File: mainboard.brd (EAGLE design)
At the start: 90.2 x 95.9 mm, 69 parts, among them J1 POWER_JACKPTH_LOCK, T1 SINGLE_NCHAN_FET, T2 MOSFET_PCHAN_20A, T3 SINGLE_NCHAN_FET, T4 MOSFET_PCHAN_20A, T5 SINGLE_NCHAN_FET, T6 MOSFET_PCHAN_20A, T7 MOSFET_PCHAN_20A, T8 SINGLE_NCHAN_FET, U1 MURATA_REG_OKL-T3-W12, U2 TEENSY_3.0+4, U3 RFM23BP, U4 HMC5883LSMD, U5 ITG-3200, U7 CURRENT_MAX4372, U8 CURRENT_MAX4372

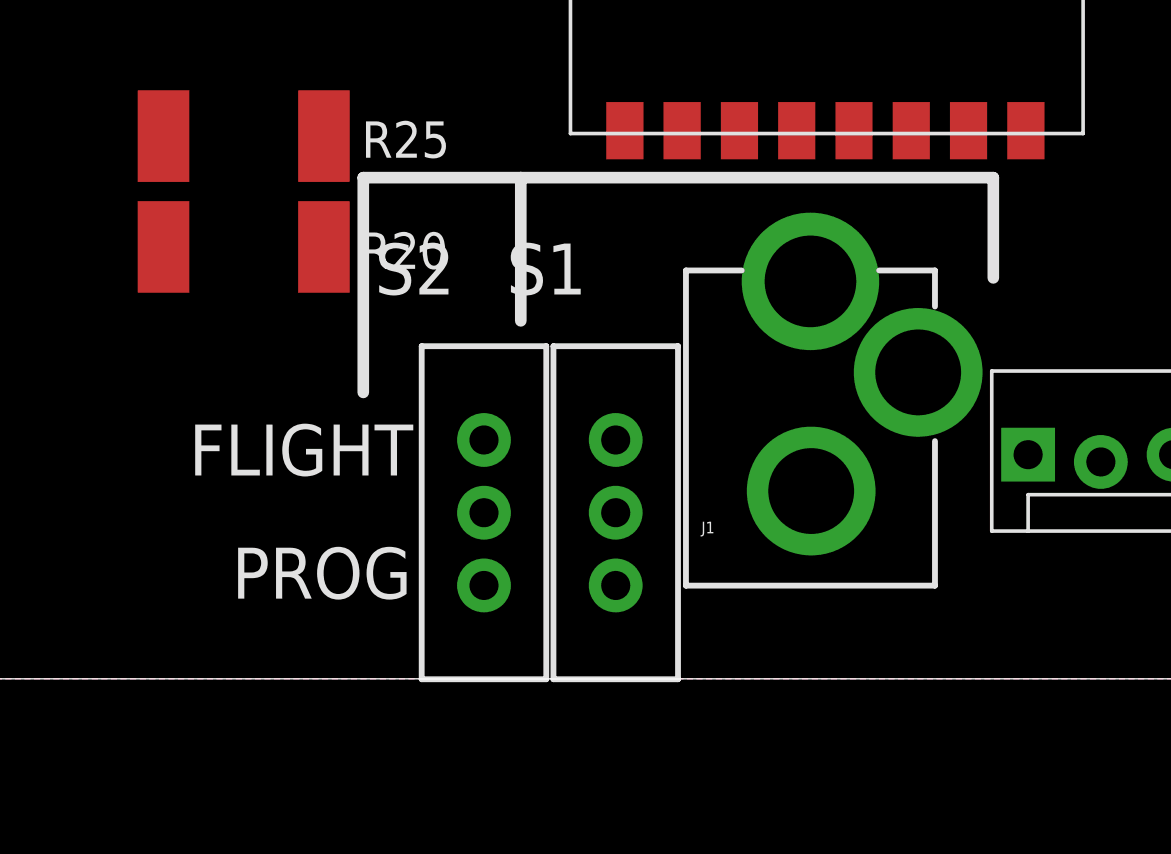
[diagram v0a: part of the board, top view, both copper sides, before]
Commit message: DPDT Switch for programming mode
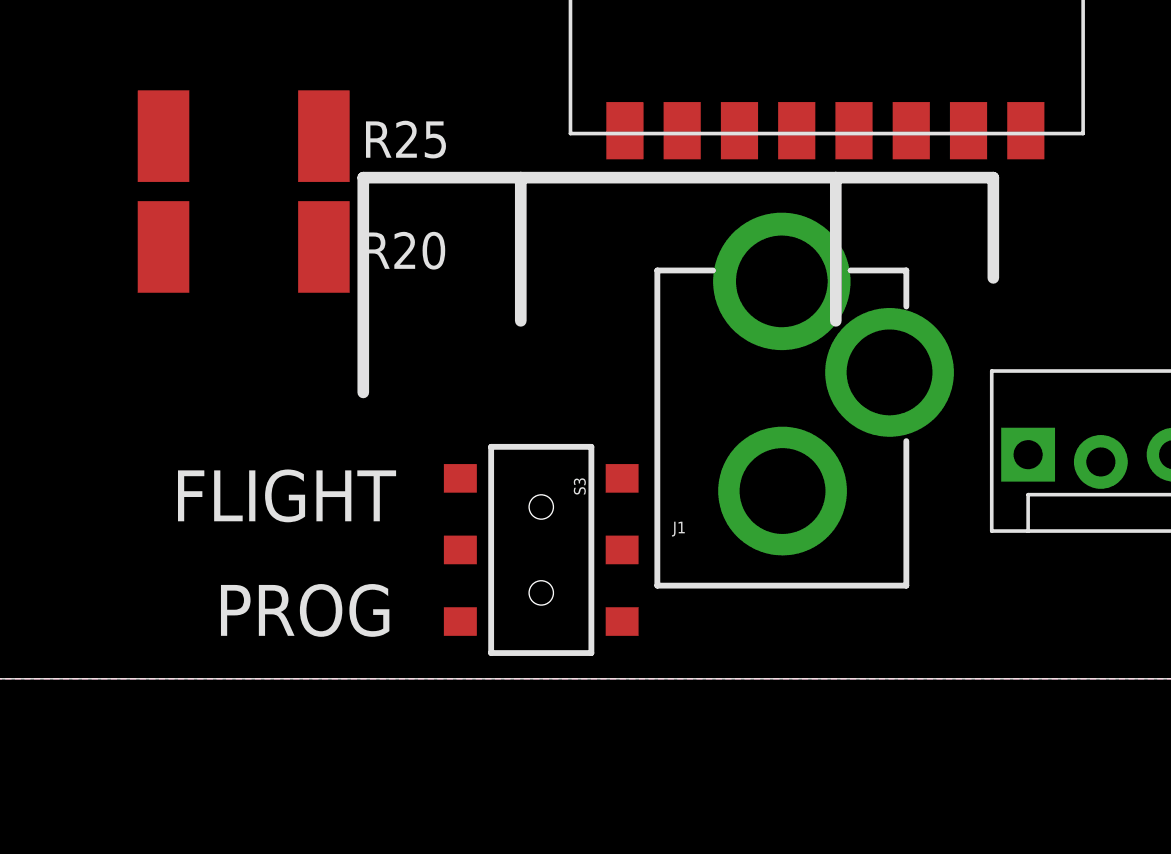
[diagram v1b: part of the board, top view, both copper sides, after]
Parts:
- removed S1, S2: (no value), SparkFun-Electromechanical:SWITCH-SPDT
- added S3: DPDT, SparkFun-Electromechanical:AYZ0202
- R14: value 10k -> 4.7k
- moved J1 1.00 mm to (48.7, 0.00)
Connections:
- net N$11: now also S3.3; no longer S1.2
- net N$13: now also S3.6; no longer S2.2
- net PGM_RST: now also S3.2; no longer S1.3
- net PGM_VCC: now also S3.5; no longer S2.3
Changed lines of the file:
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@@
 <wire x1="34.085" y1="10" x2="34.085" y2="17.5" width="0.4064" layer="21"/>
 <wire x1="34.085" y1="17.5" x2="39.585" y2="17.5" width="0.4064" layer="21"/>
-<wire x1="39.585" y1="17.5" x2="56.085" y2="17.5" width="0.4064" layer="21"/>
+<wire x1="39.585" y1="17.5" x2="50.585" y2="17.5" width="0.4064" layer="21"/>
+<wire x1="50.585" y1="17.5" x2="56.085" y2="17.5" width="0.4064" layer="21"/>
 <wire x1="56.085" y1="17.5" x2="56.085" y2="14" width="0.4064" layer="21"/>
 <wire x1="34.085" y1="95.885" x2="34.085" y2="78.385" width="0.4064" layer="21"/>
 <wire x1="56.085" y1="78.385" x2="56.085" y2="95.885" width="0.4064" layer="21"/>
-<text x="29.5" y="2.8" size="1.778" layer="21">PROG</text>
-<text x="28" y="7.1" size="1.778" layer="21">FLIGHT</text>
+<text x="28.9" y="1.5" size="1.778" layer="21">PROG</text>
+<text x="27.4" y="5.5" size="1.778" layer="21">FLIGHT</text>
+<wire x1="50.585" y1="12.5" x2="50.585" y2="17.5" width="0.4064" layer="21"/>
 </plain>
 <attributes>
@@
 <element name="R12" library="SparkFun-Resistors" package="0805" value="10K" x="-57" y="-62.4"/>
 <element name="R13" library="SparkFun-Resistors" package="0805" value="4.7K" x="-54" y="-62.4"/>
-<element name="J1" library="SparkFun-Connectors" package="POWER_JACK_PTH_LOCK" value="POWER_JACKPTH_LOCK" x="49.7" y="0">
-<attribute name="PROD_ID" value="PRT-00119" x="49.7" y="0" size="1.778" layer="27" display="off"/>
+<element name="J1" library="SparkFun-Connectors" package="POWER_JACK_PTH_LOCK" value="POWER_JACKPTH_LOCK" x="48.7" y="0">
+<attribute name="PROD_ID" value="PRT-00119" x="48.7" y="0" size="1.778" layer="27" display="off"/>
 </element>
 <element name="U$3" library="SparkFun-Boards" package="ARDUINO_PRO_MINI" value="ARDUINO_PRO_MINI" x="74" y="25" rot="R180"/>
-<element name="R14" library="SparkFun-Resistors" package="0805" value="10k" x="-95.9" y="-62.4"/>
-<element name="S1" library="SparkFun-Electromechanical" package="SWITCH-SPDT" value="" x="42.9" y="5.8"/>
-<element name="S2" library="SparkFun-Electromechanical" package="SWITCH-SPDT" value="" x="38.3" y="5.8"/>
+<element name="R14" library="SparkFun-Resistors" package="0805" value="4.7k" x="-95.9" y="-62.4"/>
+<element name="S3" library="SparkFun-Electromechanical" package="AYZ0202" value="DPDT" x="40.3" y="4.5" rot="R270">
+<attribute name="PROD_ID" value="SWCH-08179" x="40.3" y="4.5" size="1.778" layer="27" rot="R270" display="off"/>
+</element>
 </elements>
 <signals>
@@
 <contactref element="ST1" pad="1"/>
 <contactref element="J1" pad="PWR"/>
-<wire x1="19.23" y1="13.9322" x2="49.7" y2="13.8778" width="0" layer="19" extent="1-1"/>
+<wire x1="19.23" y1="13.9322" x2="48.7" y2="13.8778" width="0" layer="19" extent="1-1"/>
 <wire x1="12.09" y1="17.7878" x2="19.23" y2="13.9322" width="0" layer="19" extent="1-1"/>
 <wire x1="12.09" y1="24.7878" x2="12.09" y2="17.7878" width="0" layer="19" extent="1-1"/>
@@
 <contactref element="J1" pad="GNDBREAK"/>
 <contactref element="J1" pad="GND"/>
-<wire x1="49.7254" y1="6.557" x2="53.4616" y2="10.7" width="0" layer="19" extent="1-1"/>
-<wire x1="12.6222" y1="8" x2="49.7254" y2="6.557" width="0" layer="19" extent="1-1"/>
+<wire x1="48.7254" y1="6.557" x2="52.4616" y2="10.7" width="0" layer="19" extent="1-1"/>
+<wire x1="12.6222" y1="8" x2="48.7254" y2="6.557" width="0" layer="19" extent="1-1"/>
 <wire x1="12.09" y1="13.9322" x2="12.6222" y2="8" width="0" layer="19" extent="1-1"/>
 <wire x1="12.09" y1="20.9322" x2="12.09" y2="13.9322" width="0" layer="19" extent="1-1"/>
@@
 <signal name="PGM_VCC">
 <contactref element="U$3" pad="21"/>
-<contactref element="S2" pad="3"/>
-<wire x1="38.3" y1="3.26" x2="66.38" y2="19.92" width="0" layer="19" extent="1-1"/>
+<contactref element="S3" pad="5"/>
+<wire x1="66.38" y1="19.92" x2="37.475" y2="4.5" width="0" layer="19" extent="1-1"/>
 </signal>
 <signal name="N$11">
 <contactref element="U2" pad="23/A9"/>
-<contactref element="S1" pad="2"/>
-<wire x1="42.9" y1="5.8" x2="52.705" y2="85.89" width="0" layer="19" extent="1-1"/>
+<contactref element="S3" pad="3"/>
+<wire x1="52.705" y1="85.89" x2="43.125" y2="2" width="0" layer="19" extent="1-1"/>
 </signal>
 <signal name="PGM_RST">
 <contactref element="U$3" pad="22"/>
-<contactref element="S1" pad="3"/>
-<wire x1="42.9" y1="3.26" x2="66.38" y2="17.38" width="0" layer="19" extent="1-1"/>
+<contactref element="S3" pad="2"/>
+<wire x1="66.38" y1="17.38" x2="43.125" y2="4.5" width="0" layer="19" extent="1-1"/>
 </signal>
 <signal name="N$13">
-<contactref element="S2" pad="2"/>
 <contactref element="U2" pad="VUSB"/>
-<wire x1="38.3" y1="5.8" x2="50.165" y2="90.97" width="0" layer="19" extent="1-1"/>
+<contactref element="S3" pad="6"/>
+<wire x1="50.165" y1="90.97" x2="37.475" y2="2" width="0" layer="19" extent="1-1"/>
 </signal>
 </signals>

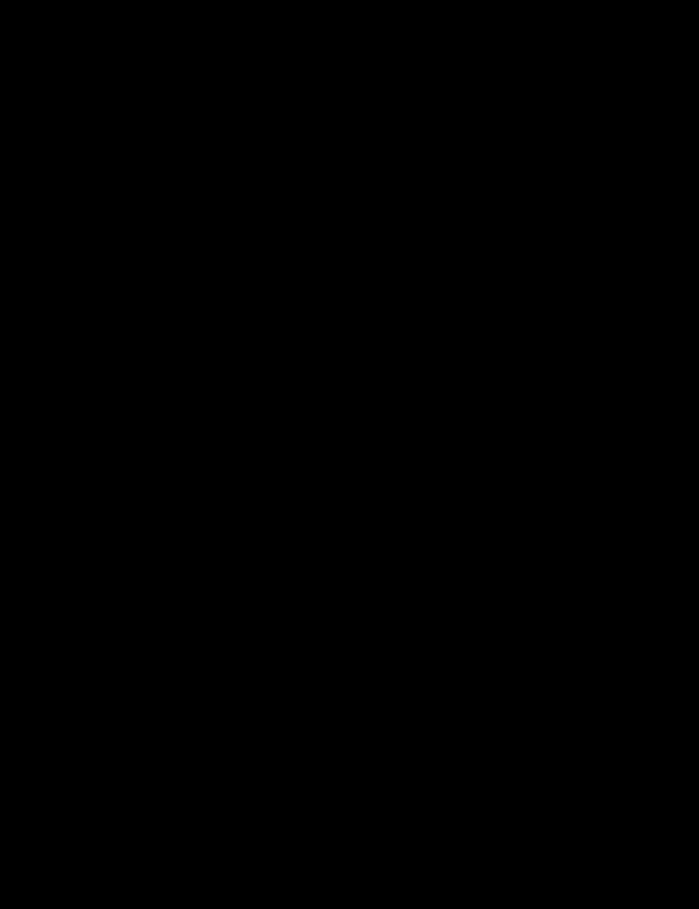
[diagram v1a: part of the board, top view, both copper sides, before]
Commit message: added piksi gps connector and enable circuitry. Added molex library
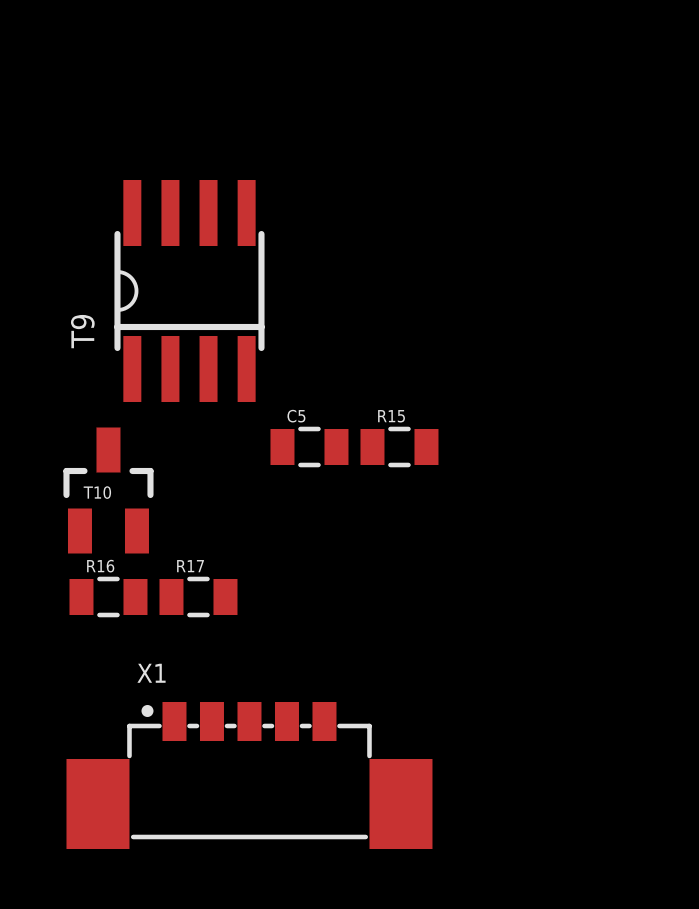
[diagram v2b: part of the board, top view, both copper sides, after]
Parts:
- added C5: .1uF, SparkFun-Capacitors:0805
- added R15: 3K3, SparkFun-Resistors:0805
- added R16: 10K, SparkFun-Resistors:0805
- added R17: 4.7K, SparkFun-Resistors:0805
- added T10: SINGLE_NCHAN_FET, phonesat:SOT23-3
- added T9: MOSFET_PCHAN_20A, phonesat:SO8
- added X1: (no value), pel_molex:PB-53398-05
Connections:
- new net ENAB_GPS: R16.1, R17.2, U2.17/A3
- new net GPS_PWR: T9.5, T9.6, T9.7, T9.8, X1.5
- new net N$10: C5.1, R16.2, T10.1
- new net N$12: R15.1, T10.3, T9.4
- net 5V: now also R15.2, T9.1, T9.2, T9.3
- net GND: now also C5.2, R17.1, T10.2, X1.1
- net UART3_RX: now also X1.3
- net UART3_TX: now also X1.2

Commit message: Schematic clean-up
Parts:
- added FRAME1, FRAME2, FRAME3: FRAME-LETTER, SparkFun-Aesthetics:CREATIVE_COMMONS
- X1: device pel_molex:PB-53398-05 -> pel_molex:PB-53261-05
- moved T9 32.7 mm to (-93.2, -106.9)
- moved C5 32.7 mm to (-89.2, -112.1)
- moved R15 32.7 mm to (-86.2, -112.1)
- moved R16 32.7 mm to (-95.9, -117.1)
- moved R17 32.7 mm to (-92.9, -117.1)
- moved T10 32.7 mm to (-95.9, -113.6)
- moved X1 22.0 mm to (-91.2, -67.8)
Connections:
- net N$11: now also S3.1; no longer S3.3
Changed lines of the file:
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@@
 <attribute name="PROD_ID" value="SWCH-08179" x="40.3" y="4.5" size="1.778" layer="27" rot="R270" display="off"/>
 </element>
-<element name="T9" library="phonesat" package="SO8" value="MOSFET_PCHAN_20A" x="-93.2" y="-74.2"/>
-<element name="T10" library="phonesat" package="SOT23-3" value="SINGLE_NCHAN_FET" x="-95.9" y="-80.9"/>
-<element name="R15" library="SparkFun-Resistors" package="0805" value="3K3" x="-86.2" y="-79.4"/>
-<element name="C5" library="SparkFun-Capacitors" package="0805" value=".1uF" x="-89.2" y="-79.4"/>
-<element name="R16" library="SparkFun-Resistors" package="0805" value="10K" x="-95.9" y="-84.4"/>
-<element name="R17" library="SparkFun-Resistors" package="0805" value="4.7K" x="-92.9" y="-84.4"/>
-<element name="X1" library="pel_molex" package="PB-53398-05" value="" x="-91.2" y="-89.8"/>
+<element name="X1" library="pel_molex" package="PB-53261-05" value="" x="-91.2" y="-67.8"/>
+<element name="FRAME1" library="SparkFun-Aesthetics" package="CREATIVE_COMMONS" value="FRAME-LETTER" x="-76.5" y="-79"/>
+<element name="FRAME2" library="SparkFun-Aesthetics" package="CREATIVE_COMMONS" value="FRAME-LETTER" x="-76.5" y="-87.5"/>
+<element name="FRAME3" library="SparkFun-Aesthetics" package="CREATIVE_COMMONS" value="FRAME-LETTER" x="-76.5" y="-96"/>
+<element name="T9" library="phonesat" package="SO8" value="MOSFET_PCHAN_20A" x="-93.2" y="-106.9"/>
+<element name="T10" library="phonesat" package="SOT23-3" value="SINGLE_NCHAN_FET" x="-95.9" y="-113.6"/>
+<element name="R15" library="SparkFun-Resistors" package="0805" value="3K3" x="-86.2" y="-112.1"/>
+<element name="C5" library="SparkFun-Capacitors" package="0805" value=".1uF" x="-89.2" y="-112.1"/>
+<element name="R16" library="SparkFun-Resistors" package="0805" value="10K" x="-95.9" y="-117.1"/>
+<element name="R17" library="SparkFun-Resistors" package="0805" value="4.7K" x="-92.9" y="-117.1"/>
 </elements>
 <signals>
@@
 <contactref element="U$3" pad="4"/>
 <contactref element="R14" pad="1"/>
+<contactref element="X1" pad="1"/>
 <contactref element="T10" pad="2"/>
 <contactref element="C5" pad="2"/>
 <contactref element="R17" pad="1"/>
-<contactref element="X1" pad="1"/>
-<wire x1="-93.8" y1="-84.4" x2="-93.7" y2="-88.55" width="0" layer="19" extent="1-1"/>
-<wire x1="-94.95" y1="-82.2" x2="-93.8" y2="-84.4" width="0" layer="19" extent="1-1"/>
-<wire x1="-88.3" y1="-79.4" x2="-94.95" y2="-82.2" width="0" layer="19" extent="1-1"/>
-<wire x1="-96.8" y1="-62.4" x2="-88.3" y2="-79.4" width="0" layer="19" extent="1-1"/>
-<wire x1="-54.9" y1="-62.4" x2="-88.3" y2="-79.4" width="0" layer="19" extent="1-1"/>
-<wire x1="-56.05" y1="-60.2" x2="-54.9" y2="-62.4" width="0" layer="19" extent="1-1"/>
+<wire x1="-93.8" y1="-117.1" x2="-94.95" y2="-114.9" width="0" layer="19" extent="1-1"/>
+<wire x1="-88.3" y1="-112.1" x2="-94.95" y2="-114.9" width="0" layer="19" extent="1-1"/>
+<wire x1="-93.7" y1="-66.7" x2="-88.3" y2="-112.1" width="0" layer="19" extent="1-1"/>
+<wire x1="-96.8" y1="-62.4" x2="-93.7" y2="-66.7" width="0" layer="19" extent="1-1"/>
+<wire x1="-56.05" y1="-60.2" x2="-93.7" y2="-66.7" width="0" layer="19" extent="1-1"/>
+<wire x1="-54.9" y1="-62.4" x2="-56.05" y2="-60.2" width="0" layer="19" extent="1-1"/>
 <wire x1="-49.4" y1="-57.4" x2="-56.05" y2="-60.2" width="0" layer="19" extent="1-1"/>
 <wire x1="-52.3" y1="1.8" x2="-49.4" y2="-57.4" width="0" layer="19" extent="1-1"/>
@@
 <wire x1="59.43" y1="72" x2="61.37" y2="73.81" width="0" layer="19" extent="1-1"/>
 <wire x1="63.43" y1="66.79" x2="63" y2="70.47" width="0" layer="19" extent="1-1"/>
+<wire x1="42.545" y1="60.49" x2="59.43" y2="72" width="0" layer="19" extent="1-1"/>
 <wire x1="27.08" y1="30.4901" x2="42.545" y2="60.49" width="0" layer="19" extent="1-1"/>
 <wire x1="25.47" y1="30.49" x2="27.08" y2="30.4901" width="0" layer="19" extent="1-1"/>
@@
 <contactref element="T9" pad="2"/>
 <contactref element="R15" pad="2"/>
-<wire x1="-93.835" y1="-76.8" x2="-95.105" y2="-76.8" width="0" layer="19" extent="1-1"/>
-<wire x1="-92.565" y1="-76.8" x2="-93.835" y2="-76.8" width="0" layer="19" extent="1-1"/>
-<wire x1="-85.3" y1="-79.4" x2="-92.565" y2="-76.8" width="0" layer="19" extent="1-1"/>
-<wire x1="51.22" y1="19.14" x2="-85.3" y2="-79.4" width="0" layer="19" extent="1-1"/>
+<wire x1="-93.835" y1="-109.5" x2="-95.105" y2="-109.5" width="0" layer="19" extent="1-1"/>
+<wire x1="-92.565" y1="-109.5" x2="-93.835" y2="-109.5" width="0" layer="19" extent="1-1"/>
+<wire x1="-85.3" y1="-112.1" x2="-92.565" y2="-109.5" width="0" layer="19" extent="1-1"/>
+<wire x1="51.22" y1="19.14" x2="-85.3" y2="-112.1" width="0" layer="19" extent="1-1"/>
 <wire x1="21.7" y1="70.5" x2="51.22" y2="19.14" width="0" layer="19" extent="1-1"/>
 <wire x1="21.629" y1="74.039" x2="21.7" y2="70.5" width="0" layer="19" extent="1-1"/>
@@
 <contactref element="U2" pad="7"/>
 <contactref element="X1" pad="3"/>
-<wire x1="37.465" y1="73.19" x2="-91.2" y2="-88.55" width="0" layer="19" extent="1-1"/>
+<wire x1="37.465" y1="73.19" x2="-91.2" y2="-66.7" width="0" layer="19" extent="1-1"/>
 </signal>
 <signal name="UART3_TX">
 <contactref element="U2" pad="8"/>
 <contactref element="X1" pad="2"/>
-<wire x1="37.465" y1="70.65" x2="-92.45" y2="-88.55" width="0" layer="19" extent="1-1"/>
+<wire x1="37.465" y1="70.65" x2="-92.45" y2="-66.7" width="0" layer="19" extent="1-1"/>
 </signal>
 <signal name="RF_SDN">
@@
 <signal name="N$11">
 <contactref element="U2" pad="23/A9"/>
-<contactref element="S3" pad="3"/>
-<wire x1="52.705" y1="85.89" x2="43.125" y2="2" width="0" layer="19" extent="1-1"/>
+<contactref element="S3" pad="1"/>
+<wire x1="43.125" y1="7" x2="52.705" y2="85.89" width="0" layer="19" extent="1-1"/>
 </signal>
 <signal name="PGM_RST">
@@
 <contactref element="U2" pad="VUSB"/>
 <contactref element="S3" pad="6"/>
-<wire x1="50.165" y1="90.97" x2="37.475" y2="2" width="0" layer="19" extent="1-1"/>
+<wire x1="37.475" y1="2" x2="50.165" y2="90.97" width="0" layer="19" extent="1-1"/>
 </signal>
 <signal name="N$10">
@@
 <contactref element="C5" pad="1"/>
 <contactref element="T10" pad="1"/>
-<wire x1="-96.85" y1="-82.2" x2="-95" y2="-84.4" width="0" layer="19" extent="1-1"/>
-<wire x1="-90.1" y1="-79.4" x2="-95" y2="-84.4" width="0" layer="19" extent="1-1"/>
+<wire x1="-96.85" y1="-114.9" x2="-95" y2="-117.1" width="0" layer="19" extent="1-1"/>
+<wire x1="-90.1" y1="-112.1" x2="-95" y2="-117.1" width="0" layer="19" extent="1-1"/>
 </signal>
 <signal name="N$12">
@@
 <contactref element="T9" pad="4"/>
 <contactref element="R15" pad="1"/>
-<wire x1="-91.295" y1="-76.8" x2="-95.9" y2="-79.5" width="0" layer="19" extent="1-1"/>
-<wire x1="-87.1" y1="-79.4" x2="-91.295" y2="-76.8" width="0" layer="19" extent="1-1"/>
+<wire x1="-91.295" y1="-109.5" x2="-95.9" y2="-112.2" width="0" layer="19" extent="1-1"/>
+<wire x1="-87.1" y1="-112.1" x2="-91.295" y2="-109.5" width="0" layer="19" extent="1-1"/>
 </signal>
 <signal name="ENAB_GPS">
@@
 <contactref element="R17" pad="2"/>
 <contactref element="U2" pad="17/A3"/>
-<wire x1="-92" y1="-84.4" x2="-96.8" y2="-84.4" width="0" layer="19" extent="1-1"/>
-<wire x1="52.705" y1="70.65" x2="-92" y2="-84.4" width="0" layer="19" extent="1-1"/>
+<wire x1="-92" y1="-117.1" x2="-96.8" y2="-117.1" width="0" layer="19" extent="1-1"/>
+<wire x1="52.705" y1="70.65" x2="-92" y2="-117.1" width="0" layer="19" extent="1-1"/>
 </signal>
 <signal name="GPS_PWR">
@@
 <contactref element="T9" pad="5"/>
 <contactref element="X1" pad="5"/>
-<wire x1="-91.295" y1="-71.6" x2="-88.7" y2="-88.55" width="0" layer="19" extent="1-1"/>
-<wire x1="-92.565" y1="-71.6" x2="-91.295" y2="-71.6" width="0" layer="19" extent="1-1"/>
-<wire x1="-93.835" y1="-71.6" x2="-92.565" y2="-71.6" width="0" layer="19" extent="1-1"/>
-<wire x1="-95.105" y1="-71.6" x2="-93.835" y2="-71.6" width="0" layer="19" extent="1-1"/>
+<wire x1="-93.835" y1="-104.3" x2="-95.105" y2="-104.3" width="0" layer="19" extent="1-1"/>
+<wire x1="-92.565" y1="-104.3" x2="-93.835" y2="-104.3" width="0" layer="19" extent="1-1"/>
+<wire x1="-91.295" y1="-104.3" x2="-92.565" y2="-104.3" width="0" layer="19" extent="1-1"/>
+<wire x1="-88.7" y1="-66.7" x2="-91.295" y2="-104.3" width="0" layer="19" extent="1-1"/>
 </signal>
 </signals>

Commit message: Mainboard routing work
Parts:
- moved C30 107.5 mm to (108.9, 92.2)
- moved C32 107.5 mm to (125.5, 96.4)
- moved R27 107.5 mm to (117.1, 92.2)
- moved R28 107.5 mm to (111.4, 95.7)
- moved R6 107.5 mm to (128.9, 91.2)
- moved R7 107.5 mm to (128.9, 93.9)
- moved T1 107.5 mm to (112.7, 92.2)
- moved T2 107.5 mm to (111.5, 87.6)
- moved T5 107.5 mm to (125.4, 92.6)
- moved T6 107.5 mm to (127.3, 85.5)
- moved C1 105.9 mm to (126.9, 56.8)
- moved C2 105.9 mm to (123.4, 57.8)
- moved R9 105.9 mm to (115.3, 60.6)
- moved U1 105.9 mm to (123.4, 67.2)
- moved C3 105.9 mm to (134.2, 73.2)
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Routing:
- net GND: track 0.00 -> 44.6 mm, vias 4 -> 19
- net RF_NIRQ: track 0.00 -> 37.7 mm, vias 0 -> 1
- net SPI_SCK: track 0.00 -> 32.0 mm, vias 0 -> 1
- net RF_SDN: track 0.00 -> 24.7 mm
- net SPI_SS: track 0.00 -> 20.3 mm
- net 3.3V: track 0.00 -> 17.8 mm, vias 0 -> 6
- net SPI_MOSI: track 0.00 -> 14.8 mm
- net SPI_MISO: track 0.00 -> 10.7 mm
- net N$44: track 0.00 -> 9.31 mm
- net N$19: track 0.00 -> 7.82 mm
- net N$43: track 0.00 -> 6.51 mm
- net 5V: track 0.00 -> 6.40 mm
- net I2C_SDA: track 0.00 -> 4.93 mm
- net I2C_SCL: track 0.00 -> 4.92 mm
- net N$7: track 0.00 -> 3.54 mm
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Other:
- board text removed: "U6"
